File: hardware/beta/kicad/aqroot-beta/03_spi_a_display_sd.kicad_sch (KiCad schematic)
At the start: 17 parts, among them J1 CH280QV10-CT_50P, J2 Micro_SD_Card, U17 TPS61169DCKR

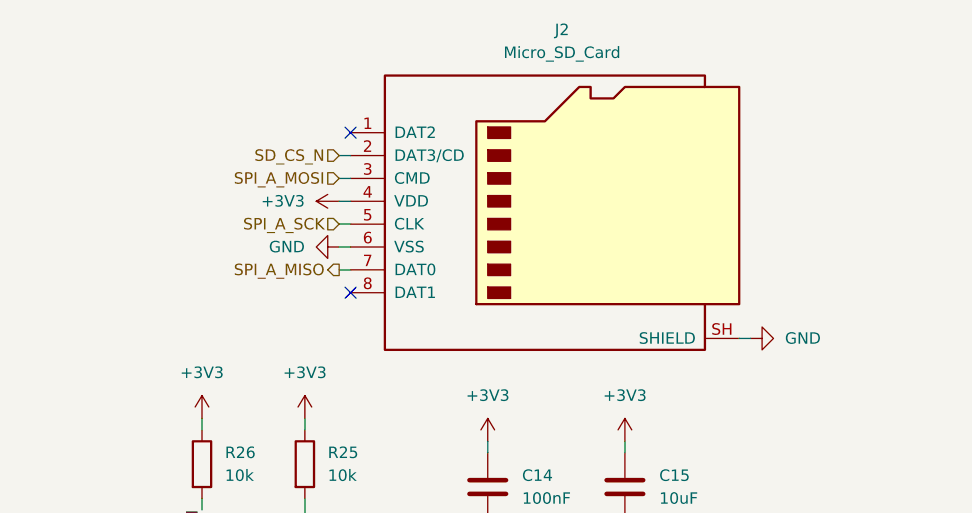
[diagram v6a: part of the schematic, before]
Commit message: Integrate physical Molex 5025700893 microSD connector at J2
Replaces the stock Connector:Micro_SD_Card symbol at J2 with the physical
11-pin Molex_5025700893 on AQROOT_Beta:Molex_5025700893. One sheet touched,
03_spi_a_display_sd. J2 is the last connector on the missing-footprint list.

ALL 11 PINS VERIFIED AGAINST AN EXPECTED MAP, not merely counted. An expected
pin-to-net table was written before validating and every logical pin compared
against the exported netlist: 11 of 11 match with zero mismatches. DAT2 and DAT1
carry explicit no-connect flags, CD/DAT3 is SD_CS_N, CMD is SPI_A_MOSI, VDD is
+3V3, CLK is SPI_A_SCK, VSS is GND, DAT0 is SPI_A_MISO, SHIELD is GND, DET-SW is
SD_CARD_DETECT_TBD and DETECT LEVER is GND.

THE OLD WIRING WAS DELETED EXPLICITLY BEFORE THE NEW SYMBOL WAS PLACED, because
past integrations showed that removing only the symbol leaves its wires behind
and silently lands new pins on wrong nets. The deletion set covered the J2
symbol, seven wires, two no-connect flags and three orphaned power symbols, and
the stock lib_symbols cache entry was removed rather than left stale. Nothing
could survive to bind a new pin to an old net.

SPI BUS A IS BYTE-IDENTICAL ACROSS THE SWAP. SPI_A_SCK still holds J1.37, J2.5
and U1.20; SPI_A_MOSI holds J1.34, J2.3 and U1.19; SPI_A_MISO holds J1.33, J2.7
and U1.21; SD_CS_N holds J2.2, R25.2 and U1.25. The +3V3 rail is unchanged at 73
pins. GND moves from 187 to 188 pins, and the difference is exactly the old
single SH terminal being replaced by pins 9 and 11 - the shell and the detect
lever, which Molex labels Vss:GROUND. Only four nets changed in the whole
project and the set of changed nets not involving J2 is EMPTY.

CARD DETECT IS CAPTURED BUT DELIBERATELY NOT ROUTED. Pin 10 goes to a named
SD_CARD_DETECT_TBD label rather than being no-connected, so the terminal is
visible and traceable, and no GPIO was allocated and the MCU pin map is
unchanged. Pin 2 remains SD_CS_N; the mechanical switch is NOT conflated w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
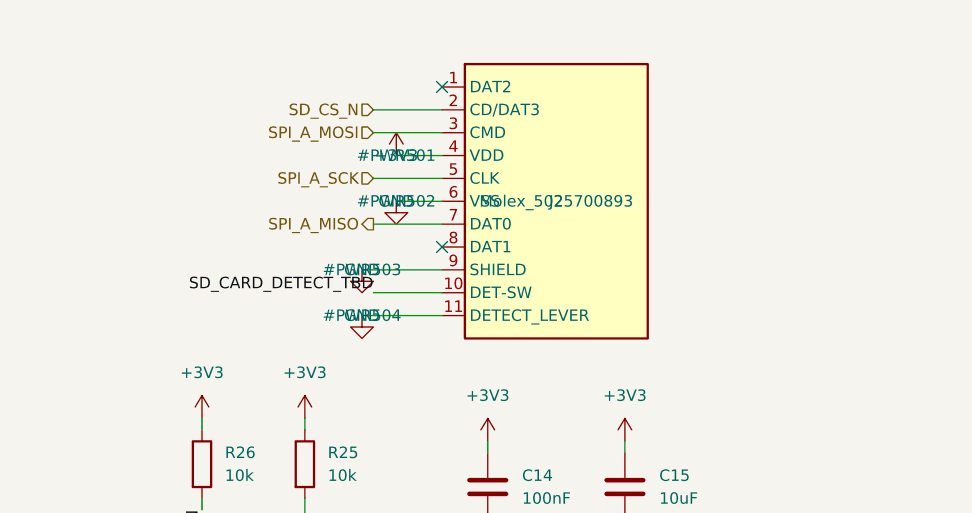
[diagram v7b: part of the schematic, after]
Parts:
- removed J2: Micro_SD_Card, symbol Connector:Micro_SD_Card
- added J2: Molex_5025700893, AQROOT_Beta:Molex_5025700893, symbol AQROOT_Beta:Molex_5025700893
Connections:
- net +3V3: now also J2.4 (VDD)
- net GND: now also J2.11 (DETECT_LEVER), J2.6 (VSS), J2.9 (SHIELD)
- net SD_CS_N: now also J2.2 (CD/DAT3)
- net SPI_A_MISO: now also J2.7 (DAT0)
- net SPI_A_MOSI: now also J2.3 (CMD)
- net SPI_A_SCK: now also J2.5 (CLK)
- new net SD_CARD_DETECT_TBD: J2.10 (DET-SW)

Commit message: AQROOT Beta: close routing blockers, add U17 VIN bypass
Closes the three blockers from the Routing Pass 1 partial. No routing was
performed; GND remains the only net carrying copper.

BAT/SYS width lock, per CTO ruling. IBAT_OCP 3.125 A is a fault trip
threshold, not a routing design current, and the floor derived from it
made U11's 0.40 mm pitch west flank unroutable. BAT_MAIN min 1.00/opt
1.50 -> min 0.60/opt 1.00 mm (1.5 A sustained, 1 oz outer, dT=10 K needs
0.525 mm). SYS_MAIN min 0.60/opt 1.00 -> min 0.50/opt 0.80 mm. Netclass
defaults follow. The wrong derivation is corrected in the rule comment so
it stops propagating. Layer policy is now written into the file: both
rails are outer-layer by policy, BAT_MAIN must not distribute on In2
(1.5 A at 0.5 oz needs 2.73 mm), and an outer width must never be
inherited onto inner copper. Necking rule unchanged, still in the
PRECEDENCE TAIL. Zero RF/E4/E5 rule lines touched.

HEADER RESERVED In1 void removed. The audit found only J5 inside it - 26
THT pads, five of them GND - and no manufacturer requirement for an In1
void. Layer set F.Cu+In1+In2+B.Cu -> F.Cu+In2+B.Cu. In1 fill 10025.8 ->
10237.0 mm2, +211.3 mm2 (+2.11%), now 91.56% of outline. The 37 x 8.5 mm
slot in the reference plane is gone and J5's five GND pins now tie
directly to the pour. ST AN5240 Rev 5 section 4.2 corroborates: "avoiding
slots in the ground plane". J5 not moved. No new DRC issue.

U9 exposed-pad grounding audited against ST AN5240 Rev 5 section 8,
retrieved via browser because curl and WebFetch both fail against st.com,
and because the archived DS12484 datasheet has no layout guidance at all.
ST asks for the pad to be tied to the ground plane by "multiple
through-vias" to "keep the total parasitic inductance low", gives no
count and no pattern, and imposes no symmetry requirement on the thermal
pad - all seven symmetry mentions in AN5240 concern the RFO/RFI
differential traces and matching network. ST's Figure 16 shows 3x3 = 9
vias as a refer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
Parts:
- added C56: 100nF, Capacitor_SMD:C_0603_1608Metric, symbol Device:C
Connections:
- net +3V3: now also C56.1
- net GND: now also C56.2
